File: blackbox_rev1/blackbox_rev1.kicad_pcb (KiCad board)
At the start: 2 copper layers, 84.1 x 78.7 mm, 15 parts, among them J1 RJ45_LED_Shielded, J2 Molex_uF_SV_06, J3 Conn_02x08_Counter_Clockwise, SW1 SW_Push, SW2 SW_Push, U1 Teensy4.1_DEV-16771, U2 TSR1-2433

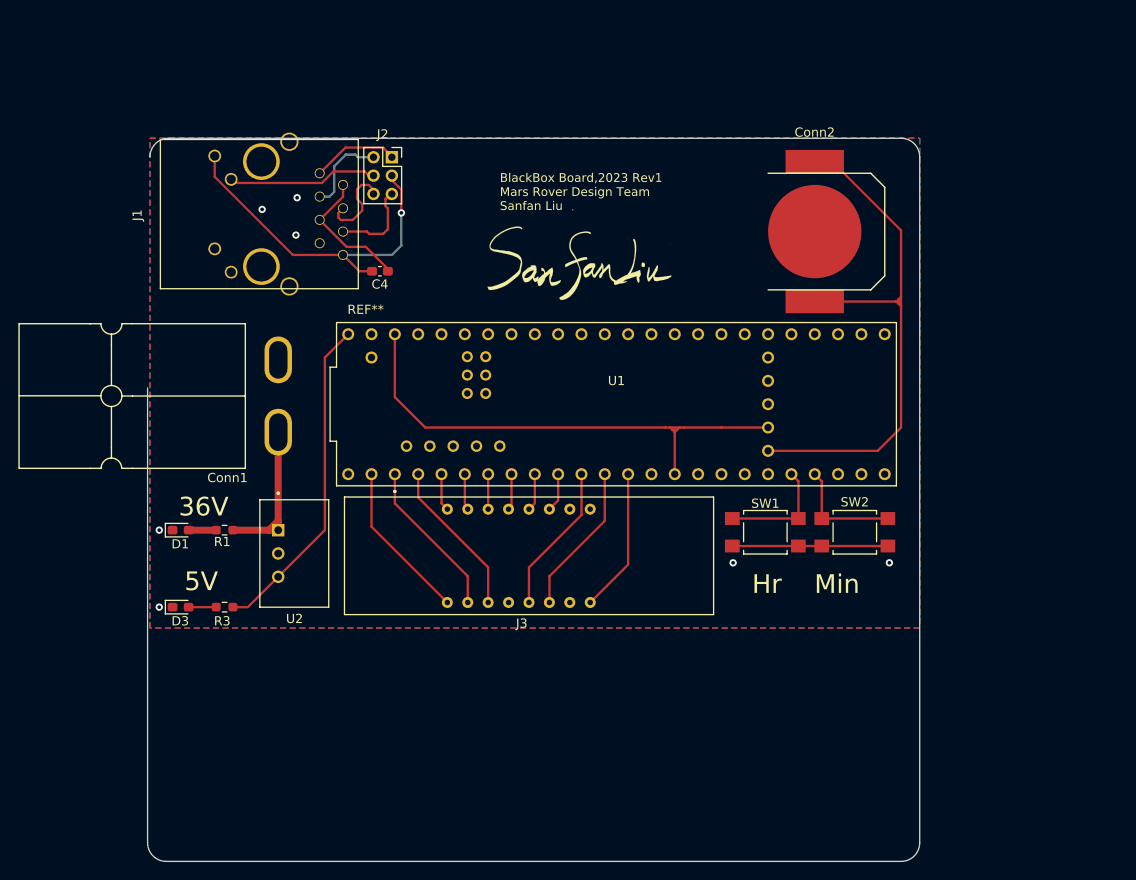
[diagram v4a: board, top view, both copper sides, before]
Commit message: add mounting holder
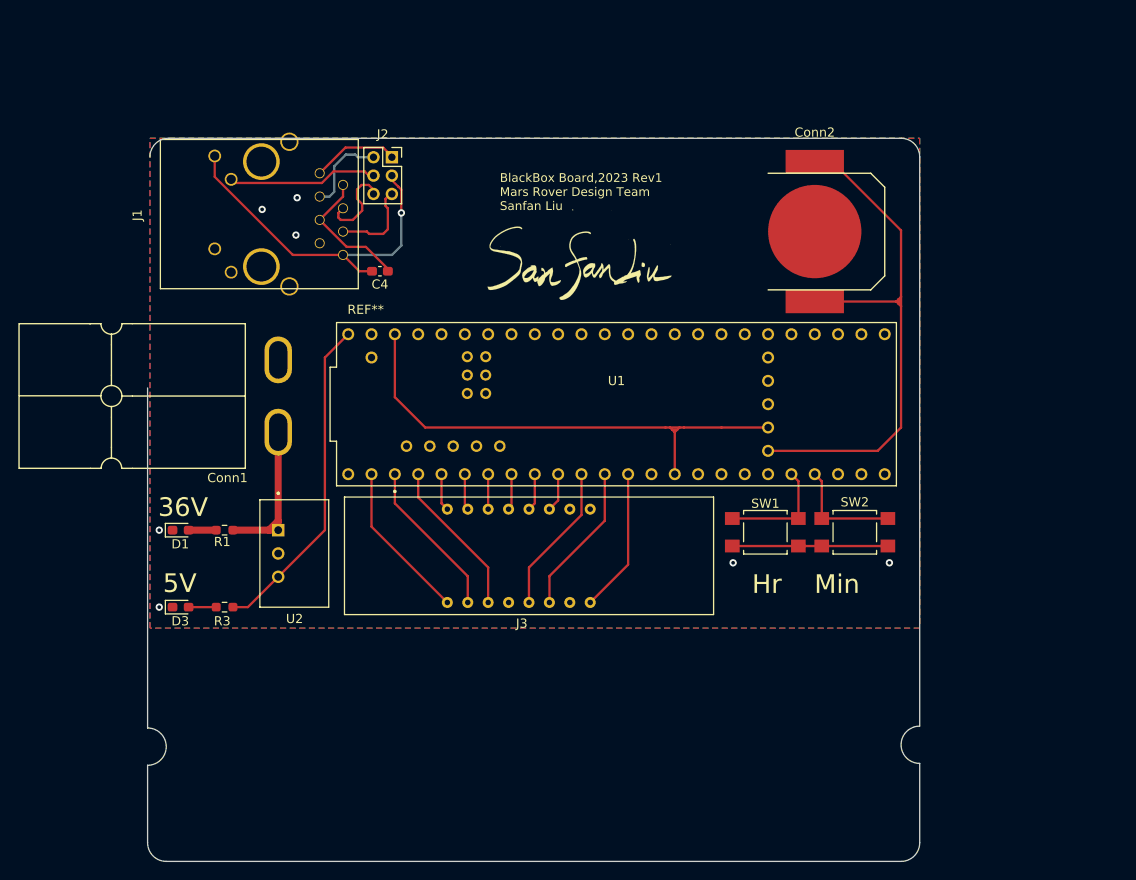
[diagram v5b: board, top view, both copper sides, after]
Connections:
- Conn2 pad 1: (no net) -> VBAT
- Conn2 pad 2: (no net) -> GND
- U1 pad VBAT: Net-(Conn2-Pad+V) -> VBAT
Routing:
- net VBAT: track 0.00 -> 64.1 mm
- net Net-(Conn2-Pad+V): track 64.1 -> 0.00 mm
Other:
- outline, holes or cut-outs redrawn
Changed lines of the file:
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@@
   (net 68 "unconnected-(J3-Pad10)")
   (net 69 "+5V")
-  (net 70 "Net-(Conn2-Pad+V)")
+  (net 70 "VBAT")
   (footprint "LED_SMD:LED_0603_1608Metric_Pad1.05x0.95mm_HandSolder" (layer "F.Cu")
     (at 60.4895 103.378)
@@
       (net 2 "GND") (pinfunction "USB_GND") (pintype "power_in"))
     (pad "VBAT" thru_hole circle locked (at 67.31 40.64) (size 1.308 1.308) (drill 0.8) (layers *.Cu *.Mask)
-      (net 70 "Net-(Conn2-Pad+V)") (pinfunction "VBAT") (pintype "passive"))
+      (net 70 "VBAT") (pinfunction "VBAT") (pintype "passive"))
     (pad "VIN" thru_hole circle locked (at 21.59 27.94) (size 1.308 1.308) (drill 0.8) (layers *.Cu *.Mask)
       (net 69 "+5V") (pinfunction "VIN") (pintype "input"))
@@
     (fp_line (start 12.446 -7.62) (end 2.794 -7.62) (layer "F.SilkS") (width 0.15))
     (fp_line (start 13.97 -6.096) (end 12.446 -7.62) (layer "F.SilkS") (width 0.15))
-    (pad "1" smd rect locked (at 0 0 270) (size 2.54 6.35) (layers "F.Cu" "F.Paste" "F.Mask"))
-    (pad "1" smd rect locked (at 15.24 0 270) (size 2.54 6.35) (layers "F.Cu" "F.Paste" "F.Mask"))
-    (pad "2" smd circle locked (at 7.62 0 270) (size 10.16 10.16) (layers "F.Cu" "F.Paste" "F.Mask"))
+    (pad "1" smd rect locked (at 0 0 270) (size 2.54 6.35) (layers "F.Cu" "F.Paste" "F.Mask")
+      (net 70 "VBAT"))
+    (pad "1" smd rect locked (at 15.24 0 270) (size 2.54 6.35) (layers "F.Cu" "F.Paste" "F.Mask")
+      (net 70 "VBAT"))
+    (pad "2" smd circle locked (at 7.62 0 270) (size 10.16 10.16) (layers "F.Cu" "F.Paste" "F.Mask")
+      (net 2 "GND"))
     (model "${MRDT_KICAD_LIBRARIES}/3D Files/MRDT_Connctors/CR1220 SMD Contact.stp"
       (offset (xyz 13.96999979 6.984999895 0))
@@
   (gr_line (start 58.928 131.064) (end 138.938 131.064) (layer "Edge.Cuts") (width 0.05))
   (gr_arc (start 57.15 54.356) (mid 57.745159 52.919159) (end 59.182 52.324) (layer "Edge.Cuts") (width 0.05))
+  (gr_arc (start 140.97 120.396) (mid 138.938 118.364) (end 140.97 116.332) (layer "Edge.Cuts") (width 0.05))
   (gr_arc (start 140.97 129.032) (mid 140.374841 130.468841) (end 138.938 131.064) (layer "Edge.Cuts") (width 0.05))
-  (gr_line (start 56.896 79.502) (end 56.896 129.032) (layer "Edge.Cuts") (width 0.05))
-  (gr_line (start 140.97 129.032) (end 140.97 54.356) (layer "Edge.Cuts") (width 0.05))
+  (gr_line (start 56.896 120.5992) (end 56.896 129.032) (layer "Edge.Cuts") (width 0.05))
+  (gr_line (start 56.896 79.502) (end 56.896 116.5352) (layer "Edge.Cuts") (width 0.05))
+  (gr_line (start 140.97 116.332) (end 140.97 54.356) (layer "Edge.Cuts") (width 0.05))
+  (gr_line (start 140.97 120.396) (end 140.97 129.032) (layer "Edge.Cuts") (width 0.05))
   (gr_line (start 59.182 52.324) (end 138.938 52.324) (layer "Edge.Cuts") (width 0.05))
+  (gr_arc (start 56.896 116.5352) (mid 58.928 118.5672) (end 56.896 120.5992) (layer "Edge.Cuts") (width 0.05))
   (gr_arc (start 58.928 131.064) (mid 57.491159 130.468841) (end 56.896 129.032) (layer "Edge.Cuts") (width 0.05))
   (gr_text "BlackBox Board,2023 Rev1\nMars Rover Design Team\nSanfan Liu" (at 95.25 58.166) (layer "F.SilkS")
@@
     (effects (font (size 2.032 2.032) (thickness 0.2286)))
   )
-  (gr_text "5V" (at 62.738 100.584) (layer "F.SilkS")
+  (gr_text "5V" (at 60.4012 100.7872) (layer "F.SilkS")
     (effects (font (size 2.032 2.032) (thickness 0.2286)))
   )
-  (gr_text "36V" (at 62.992 92.456) (layer "F.SilkS")
+  (gr_text "36V" (at 60.7568 92.5068) (layer "F.SilkS")
     (effects (font (size 2.032 2.032) (thickness 0.2286)))
   )
@@
       (effects (font (size 1 1) (thickness 0.15)))
     )
+    (format (units 3) (units_format 1) (precision 4))
+    (style (thickness 0.15) (arrow_length 1.27) (text_position_mode 0) (extension_height 0.58642) (extension_offset 0.5) keep_text_aligned)
+  )
+  (dimension (type aligned) (layer "Dwgs.User")
+    (pts (xy 56.896 118.364) (xy 56.896 120.396))
+    (height 2.4384)
+    (gr_text "0.0800 in" (at 53.3076 119.38 90) (layer "Dwgs.User")
+      (effects (font (size 1 1) (thickness 0.15)))
+    )
+    (format (units 3) (units_format 1) (precision 4))
+    (style (thickness 0.15) (arrow_length 1.27) (text_position_mode 0) (extension_height 0.58642) (extension_offset 0.5) keep_text_aligned)
+  )
+  (dimension (type aligned) (layer "Dwgs.User")
+    (pts (xy 140.97 129.032) (xy 140.97 120.396))
+    (height -2.4384)
+    (gr_text "0.3400 in" (at 137.3816 124.714 90) (layer "Dwgs.User")
+      (effects (font (size 1 1) (thickness 0.15)))
+    )
+    (format (units 3) (units_format 1) (precision 4))
+    (style (thickness 0.15) (arrow_length 1.27) (text_position_mode 0) (extension_height 0.58642) (extension_offset 0.5) keep_text_aligned)
+  )
+  (dimension (type aligned) (layer "Dwgs.User")
+    (pts (xy 56.896 120.396) (xy 56.896 129.032))
+    (height 1.625599)
+    (gr_text "0.3400 in" (at 54.120401 124.714 90) (layer "Dwgs.User")
+      (effects (font (size 1 1) (thickness 0.15)))
+    )

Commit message: added resistors to protect teensy
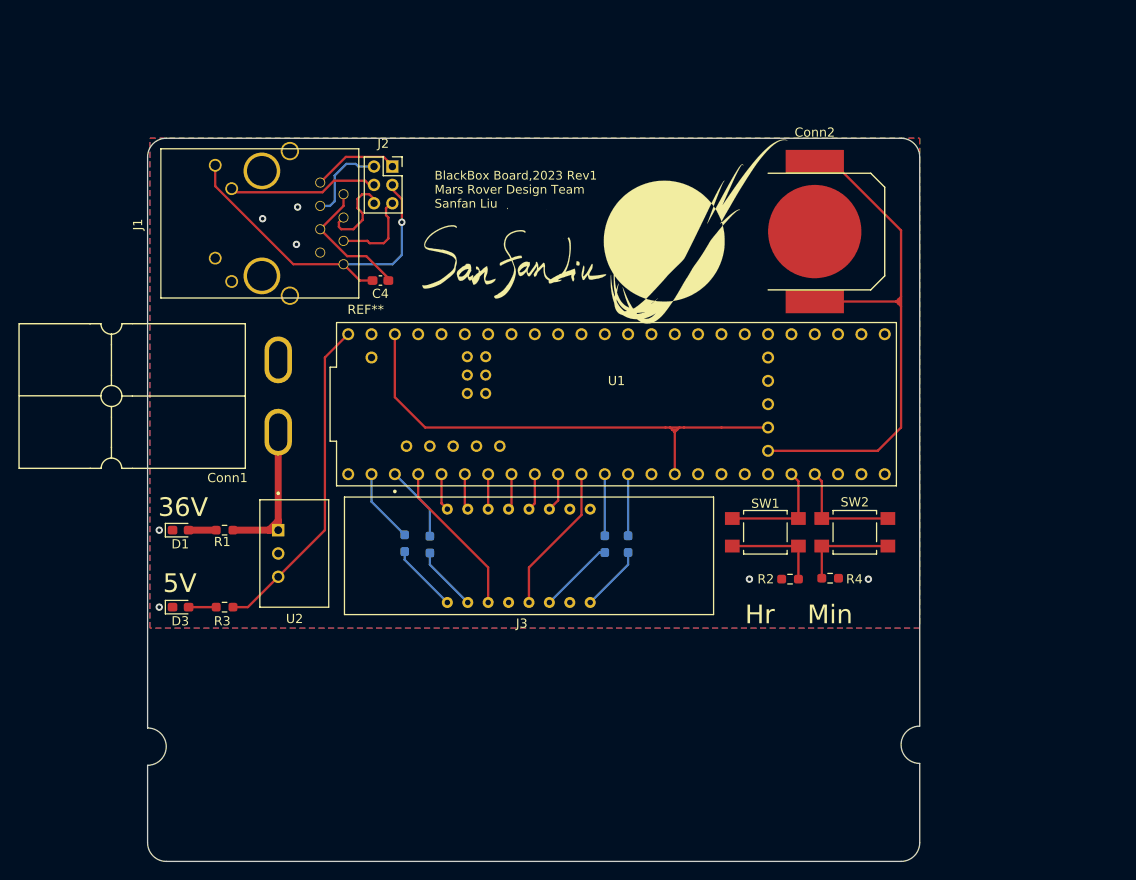
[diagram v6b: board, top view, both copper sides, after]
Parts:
- added G***: LOGO, MRDT_Silkscreens:0_MRDT_Logo_20mm, F.Cu at (116.6, 62.5)
- added R2: 4700, Resistor_SMD:R_0603_1608Metric_Pad0.98x0.95mm_HandSolder, F.Cu at (126.8, 100.3)
- added R4: 4700, Resistor_SMD:R_0603_1608Metric_Pad0.98x0.95mm_HandSolder, F.Cu at (131.2, 100.2)
- added R5: 200, Resistor_SMD:R_0603_1608Metric_Pad0.98x0.95mm_HandSolder, B.Cu at (84.9, 96.4)
- added R6: 200, Resistor_SMD:R_0603_1608Metric_Pad0.98x0.95mm_HandSolder, B.Cu at (87.6, 96.6)
- added R7: 200, Resistor_SMD:R_0603_1608Metric_Pad0.98x0.95mm_HandSolder, B.Cu at (106.7, 96.5)
- added R8: 200, Resistor_SMD:R_0603_1608Metric_Pad0.98x0.95mm_HandSolder, B.Cu at (109.2, 96.5)
- moved G*** 7.11 mm to (96.5, 65.8)
- moved J2 1.02 mm to (83.5, 55.4)
- moved C4 1.02 mm to (82.2, 67.8)
- moved J1 1.02 mm to (56.3, 61.7)
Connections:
- net VBAT renamed Net-(Conn2-Pad1)
- J3 pad 1: Display_D1_Low -> Net-(J3-Pad1)
- J3 pad 2: Display_D2_Low -> Net-(J3-Pad2)
- J3 pad 6: Display_D3_Low -> Net-(J3-Pad6)
- J3 pad 8: Display_D4_Low -> Net-(J3-Pad8)
- SW1 pad 1: GND -> Net-(R2-Pad1)
- SW2 pad 1: GND -> Net-(R4-Pad1)
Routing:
- net GND: track 17.3 -> 0.00 mm
- net Net-(R2-Pad1): track 0.00 -> 10.8 mm
- net Net-(R4-Pad1): track 0.00 -> 10.7 mm
- net Display_D3_Low: track 16.5 -> 6.71 mm
- net Display_D1_Low: track 17.4 -> 8.10 mm
- net Display_D4_Low: track 15.7 -> 6.71 mm
- net Display_D2_Low: track 17.3 -> 8.33 mm
- net Net-(J3-Pad6): track 0.00 -> 8.28 mm
- net Net-(J3-Pad1): track 0.00 -> 7.47 mm
- net Net-(J3-Pad8): track 0.00 -> 7.15 mm
- net Net-(J3-Pad2): track 0.00 -> 7.10 mm
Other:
- outline, holes or cut-outs redrawn

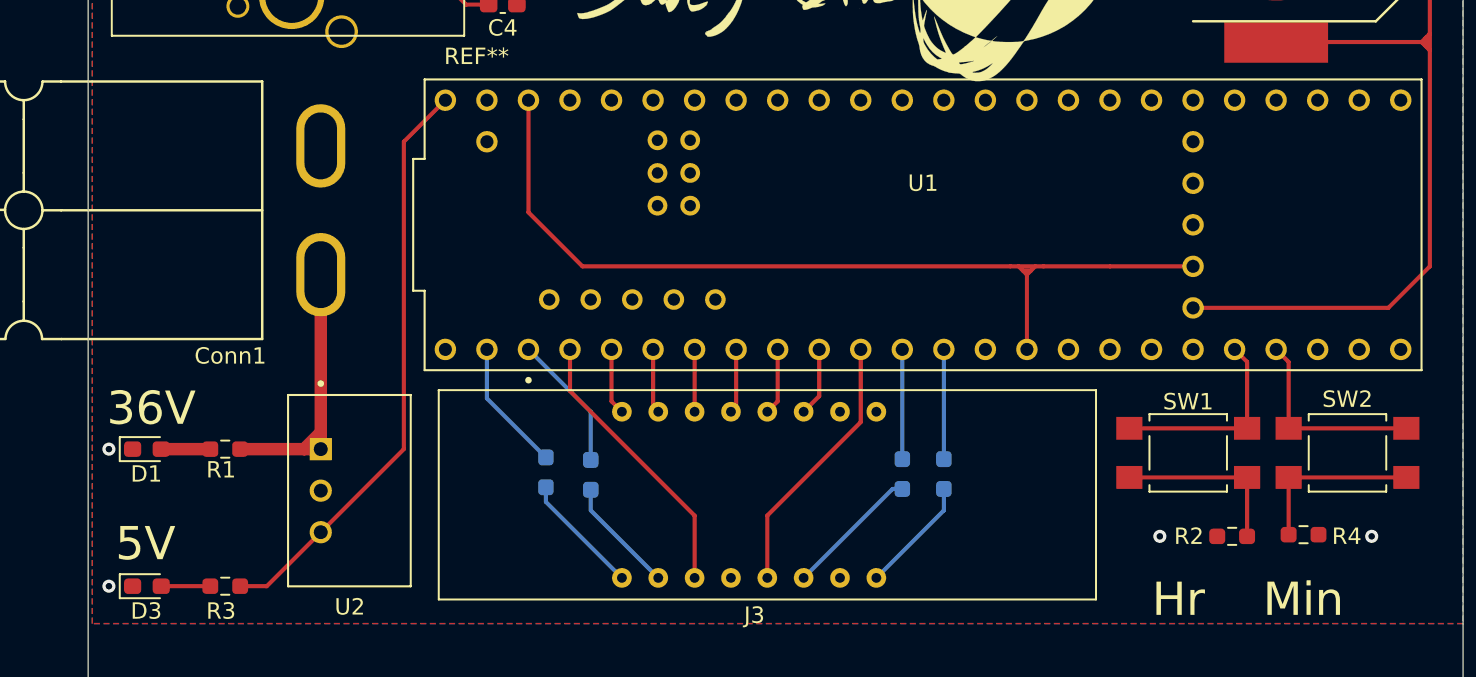
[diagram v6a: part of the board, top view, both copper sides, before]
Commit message: switch teensy and pushbutton to 3v3
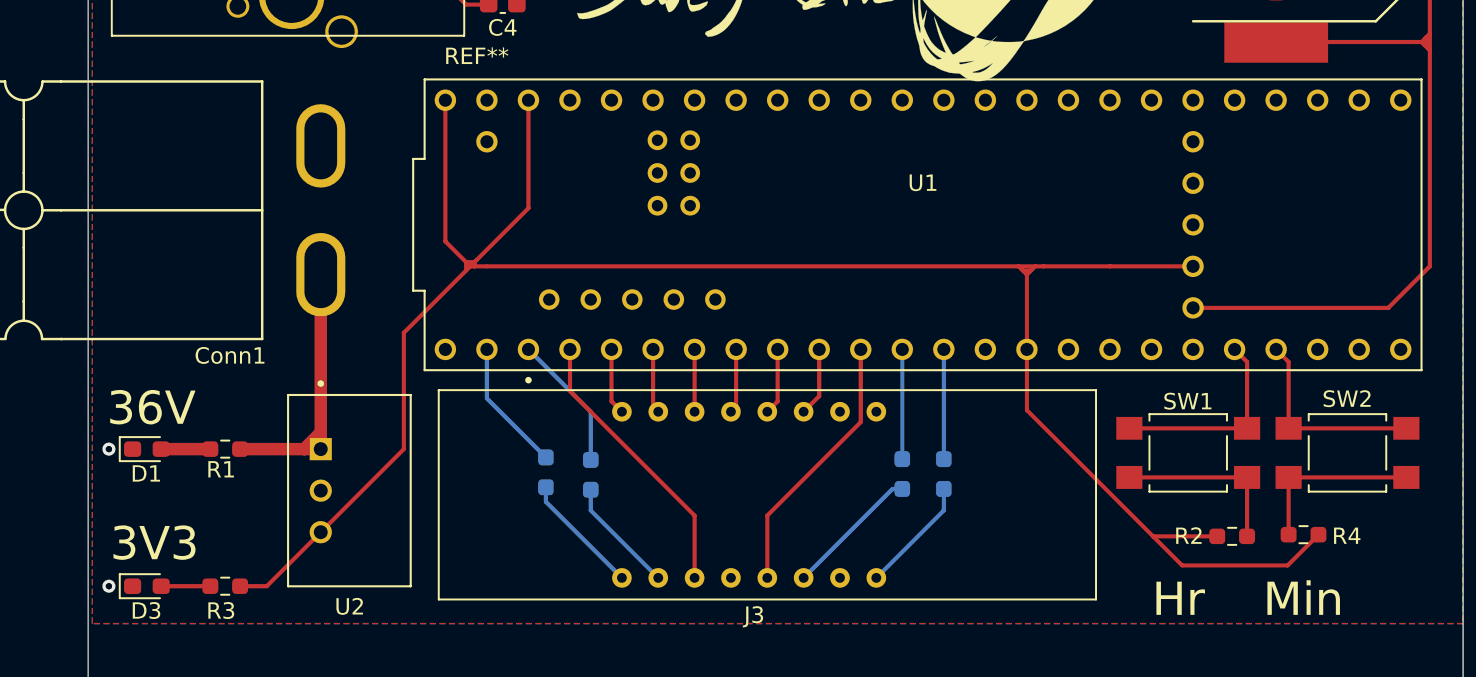
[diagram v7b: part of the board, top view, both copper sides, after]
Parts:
- R2, R4: value 4700 -> 200
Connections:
- R2 pad 2: GND -> +3V3
- R3 pad 2: +5V -> +3V3
- R4 pad 2: GND -> +3V3
- U1 pad 3.3V_1: Net-(U1-Pad3.3V_1) -> +3V3
- U1 pad 3.3V_2: Net-(U1-Pad3.3V_1) -> +3V3
- U1 pad 3.3V_3: Net-(U1-Pad3.3V_1) -> +3V3
- U1 pad VIN: +5V -> +3V3
- U2 pad 3: +5V -> +3V3
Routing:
- net +3V3: track 0.00 -> 130.9 mm
- net Net-(U1-Pad3.3V_1): track 55.4 -> 0.00 mm
- net +5V: track 35.9 -> 0.00 mm
- net GND: vias 7 -> 5
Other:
- board text added: "3V3"
- board text removed: "5V"
